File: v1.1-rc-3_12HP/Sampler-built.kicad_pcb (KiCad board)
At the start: 4 copper layers, 59 x 109 mm, 241 parts, among them J10 Eurorack_Power_10pin_Unshroud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, J11 3.5mm_Mono_Switched, J12 3.5mm_Mono_Switched, J13 3.5mm_Mono_Switched, J14 3.5mm_Mono_Switched, J15 3.5mm_Mono_Switched, J16 3.5mm_Mono_Switched, J17 3.5mm_Mono_Switched, J2 3.5mm_Mono_Switched, J3 Conn_01x04, J4 Conn_02x04, J6 3.5mm_Mono_Switched, J7 3.5mm_Mono_Switched, J8 3.5mm_Mono_Switched, J9 3.5mm_Mono_Switched, Q11 Si2347, Q12 Si2318, U1 TL072H, U10 TL072H, U11 TL072H, U12 TL072H, U13 AP62200WU-7, U14 TL072H, U15 TL072H, U16 TL072H, U2 STM32F746IE, U3 TL072H, U4 SDRAM_IS42S16400J-6BLI-TR, U5 TL072H, U6 NCP51460SN33, U8 TL072H, U9 PCM3060PW, Y1 16MHz_18pF_FA238

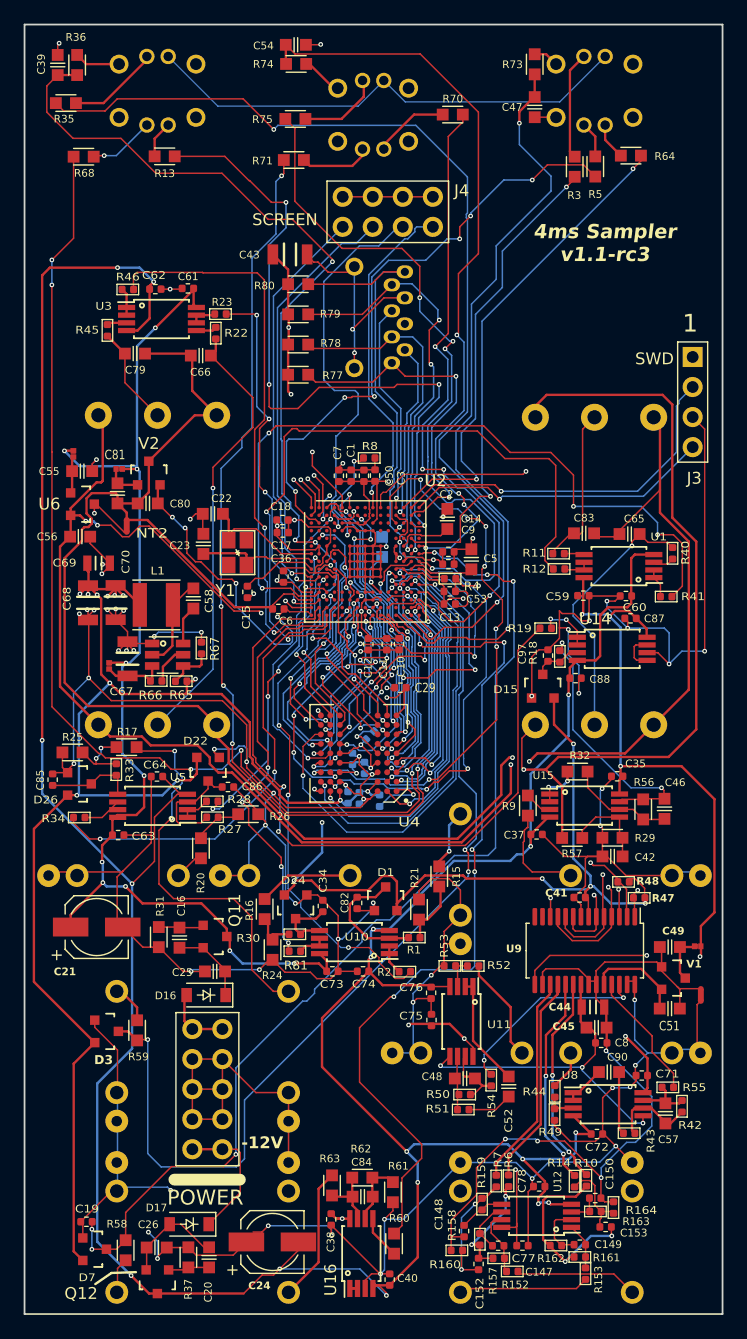
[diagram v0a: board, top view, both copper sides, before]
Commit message: Moved components to match new layout for looping delay. routing in progress
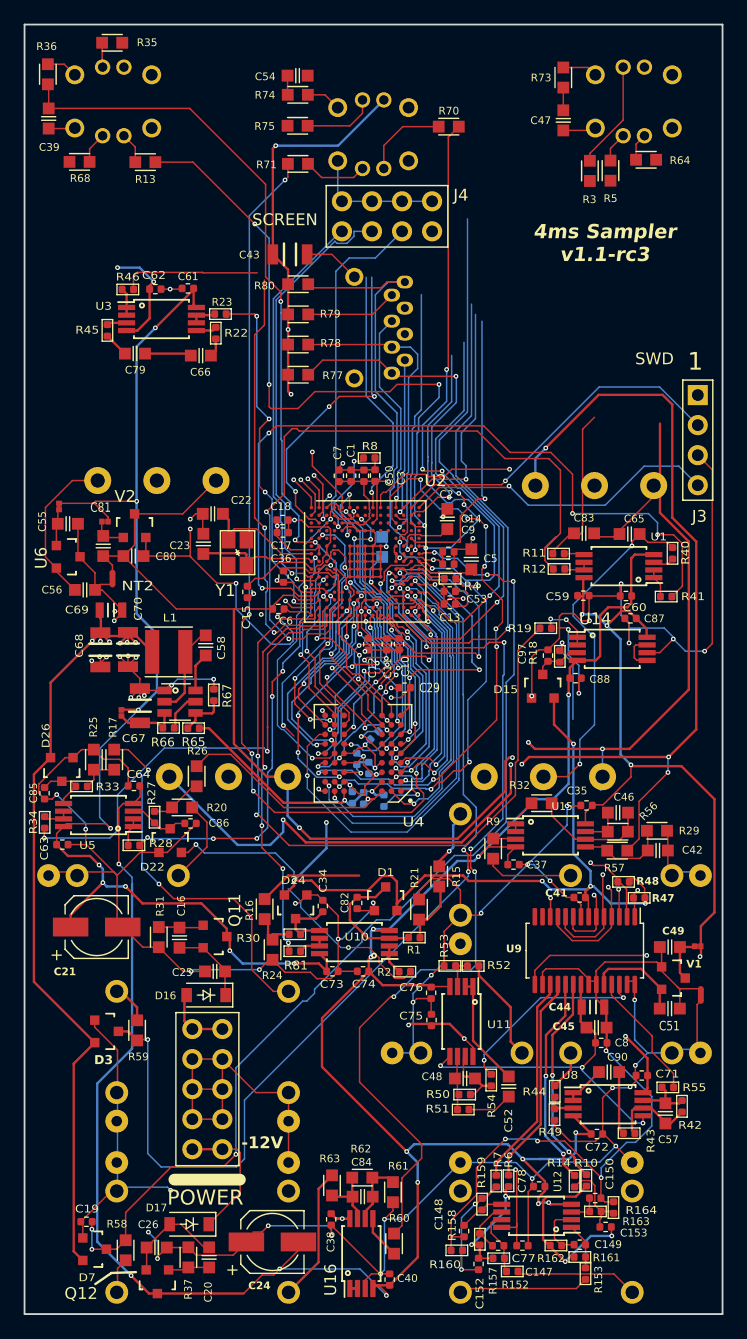
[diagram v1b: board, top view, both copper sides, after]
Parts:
- removed J6: 3.5mm_Mono_Switched, 4ms_Jack:EighthInch_PJ398SM
- moved R28 7.59 mm to (9.24, 69.4)
- moved POT_LENGTH1 7.43 mm to (17.2, 50.6)
- moved D22 6.83 mm to (12.3, 69.0), turned to 0 degrees
- moved R35 6.43 mm to (7.41, 1.54), turned to 180 degrees
- moved POT_START1 6.16 mm to (43.9, 50.6)
- moved POT_PITCH1 5.78 mm to (48.2, 26.0)
- moved POT_SAMP1 5.52 mm to (11.2, 25.6)
- moved R26 5.41 mm to (14.6, 63.5), turned to -90 degrees
- moved R27 4.89 mm to (11.0, 67.0), turned to -90 degrees
- moved C63 4.79 mm to (3.19, 69.3)
- moved R9 4.68 mm to (39.6, 69.7)
- moved U5 4.64 mm to (6.25, 66.8)
- moved JP11 4.61 mm to (2.92, 40.7)
- moved C55 4.61 mm to (3.66, 42.2)
- moved C80 4.61 mm to (9.21, 44.9)
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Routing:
- net /D7: track 102.7 -> 2.82 mm, vias 6 -> 1
- net -12VA: track 271.0 -> 209.5 mm, vias 17 -> 16
- net GND: track 562.9 -> 517.8 mm, vias 74 -> 66
- net /D10: track 88.1 -> 45.9 mm, vias 2 -> 1
- net /D12: track 64.4 -> 25.3 mm, vias 4 -> 3
- net +3V3: track 406.0 -> 369.3 mm, vias 31 -> 29
- net Net-(POT_LENGTH1-Center): track 38.2 -> 1.58 mm, vias 1 -> 0
- net VREF+: track 166.0 -> 130.3 mm, vias 6 -> 8
- net /D14: track 60.0 -> 30.4 mm, vias 4 -> 1
- net GNDADC: track 161.1 -> 134.5 mm, vias 2 -> 4
- net /D1: track 51.5 -> 27.1 mm, vias 6 -> 3
- net /D6: track 64.7 -> 42.6 mm, vias 2 -> 1
- net /D5: track 44.4 -> 24.3 mm, vias 2 -> 1
- net /D0: track 37.0 -> 20.9 mm, vias 2 -> 1
- net /A0: track 41.9 -> 28.7 mm, vias 4 -> 3
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
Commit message: routing complete, awaiting zach's review
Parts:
- moved R70 0.29 mm to (35.6, 8.61)
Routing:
- net /D7: track 2.82 -> 124.0 mm, vias 1 -> 10
- net /D10: track 45.9 -> 87.8 mm, vias 1 -> 2
- net -12VA: track 209.5 -> 250.2 mm
- net /D12: track 25.3 -> 65.7 mm, vias 3 -> 4
- net Net-(POT_LENGTH1-Center): track 1.58 -> 40.3 mm, vias 0 -> 3
- net VREF+: track 130.3 -> 167.9 mm, vias 8 -> 10
- net /D14: track 30.4 -> 64.0 mm, vias 1 -> 4
- net /D1: track 27.1 -> 50.7 mm, vias 3 -> 4
- net /D6: track 42.6 -> 65.3 mm, vias 1 -> 2
- net /D5: track 24.3 -> 44.0 mm, vias 1 -> 2
- net GND: track 517.8 -> 536.3 mm, vias 66 -> 68
- net +3V3: track 369.3 -> 386.9 mm
- net /D0: track 20.9 -> 37.4 mm, vias 1 -> 2
- net /A0: track 28.7 -> 41.4 mm, vias 3 -> 6
- net Net-(POT_SAMP1-Center): track 2.09 -> 13.9 mm
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
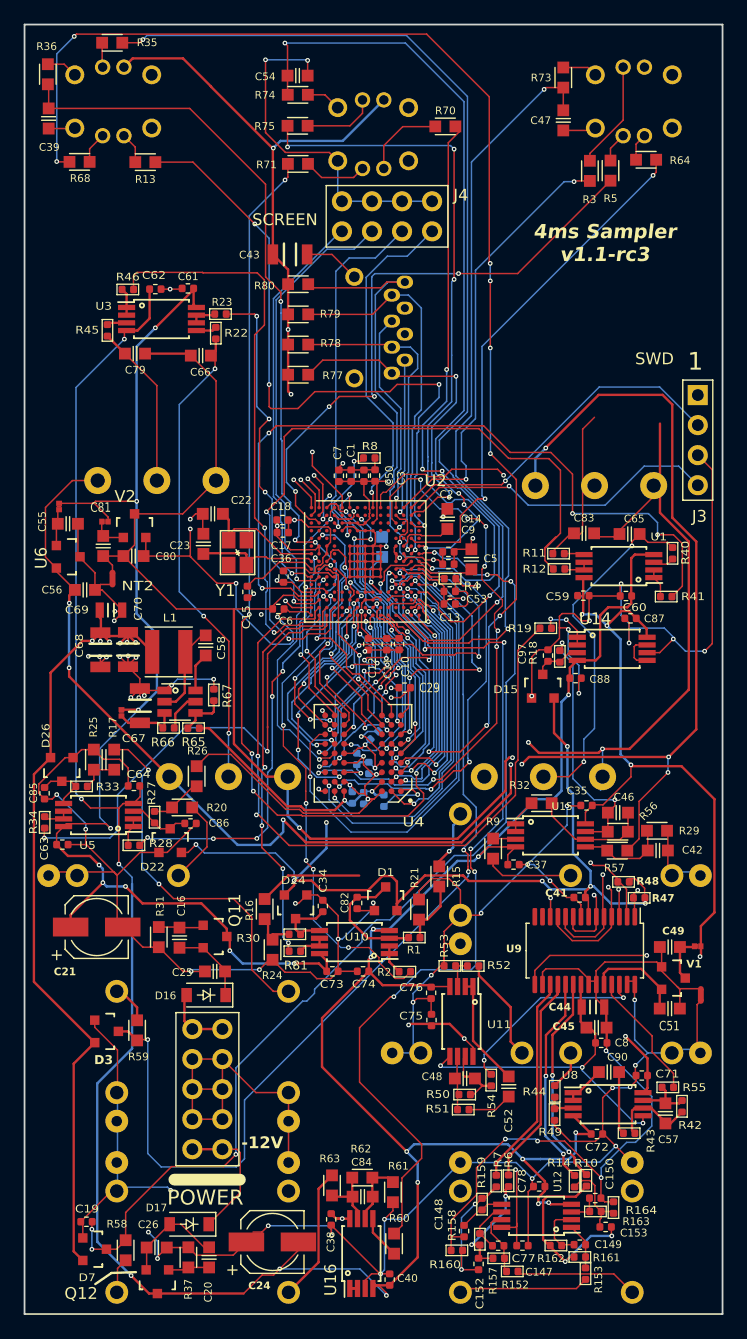
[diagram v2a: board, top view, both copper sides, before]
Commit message: started making new faceplate
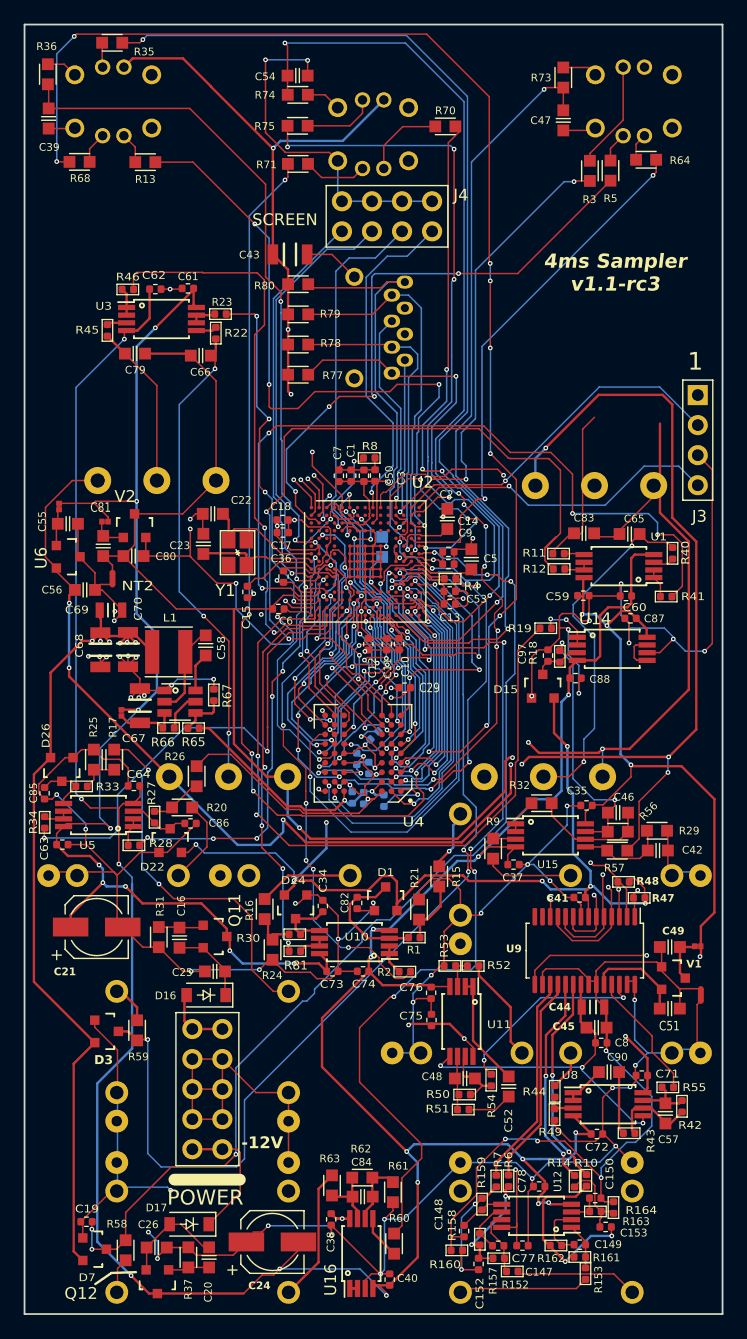
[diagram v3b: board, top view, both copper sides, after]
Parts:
- added J6: 3.5mm_Mono_Switched, 4ms_Jack:EighthInch_PJ398SM, B.Cu at (22.3, 71.9)
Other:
- board text removed: "SWD"

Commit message: cleaned up traces, will rebounce gerbers
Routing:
- net +12V: track 251.4 -> 248.0 mm
- net /D12: track 65.7 -> 63.9 mm
- net /D7: track 124.0 -> 122.3 mm
- net GND: track 536.3 -> 536.9 mm
- net /D10: track 87.8 -> 87.2 mm
- net Net-(REV_BUT1-G): track 2.08 -> 2.58 mm
